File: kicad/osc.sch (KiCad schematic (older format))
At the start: 29 parts, among them J201 power, Q201 BC557, Q202 2N3819, U201 TL082, U202 TL082, U203 TL082

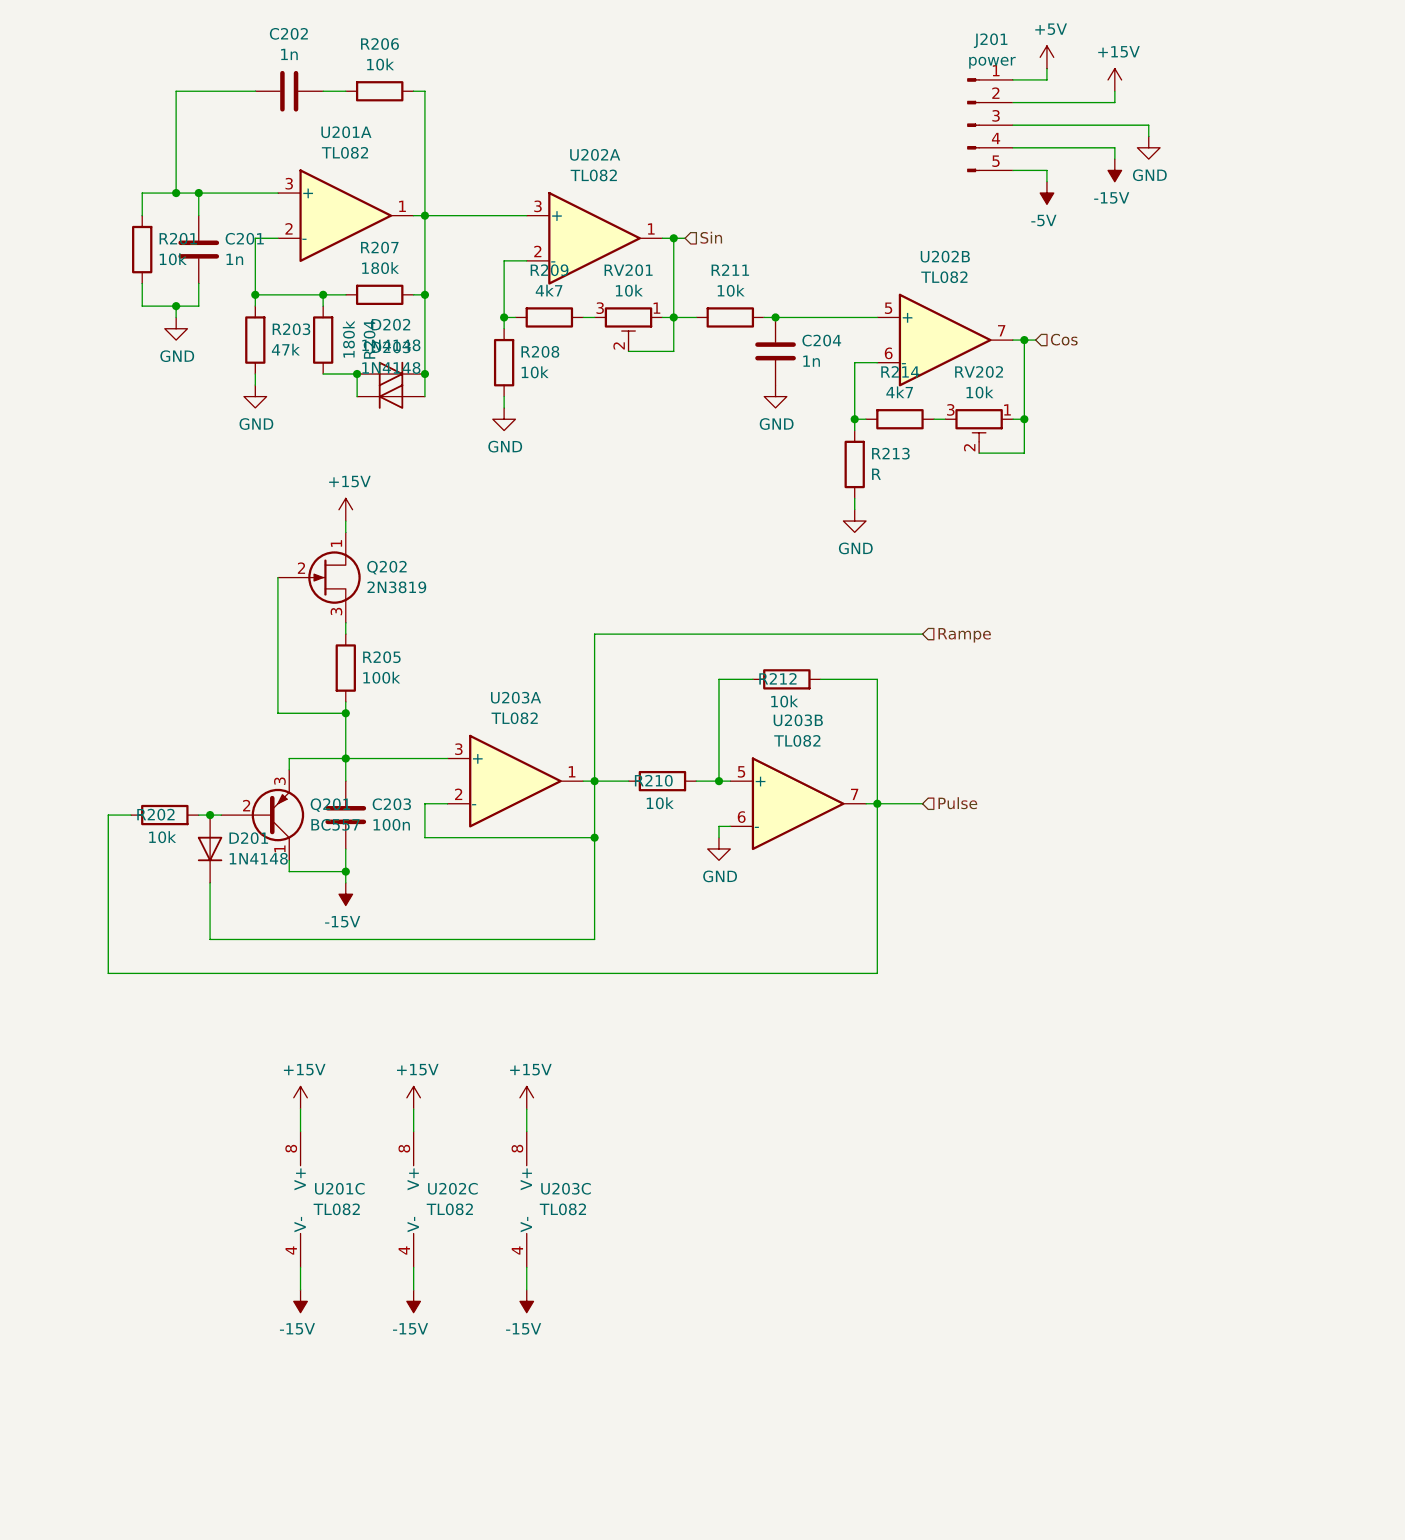
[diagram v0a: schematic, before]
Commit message: Tested oscillators
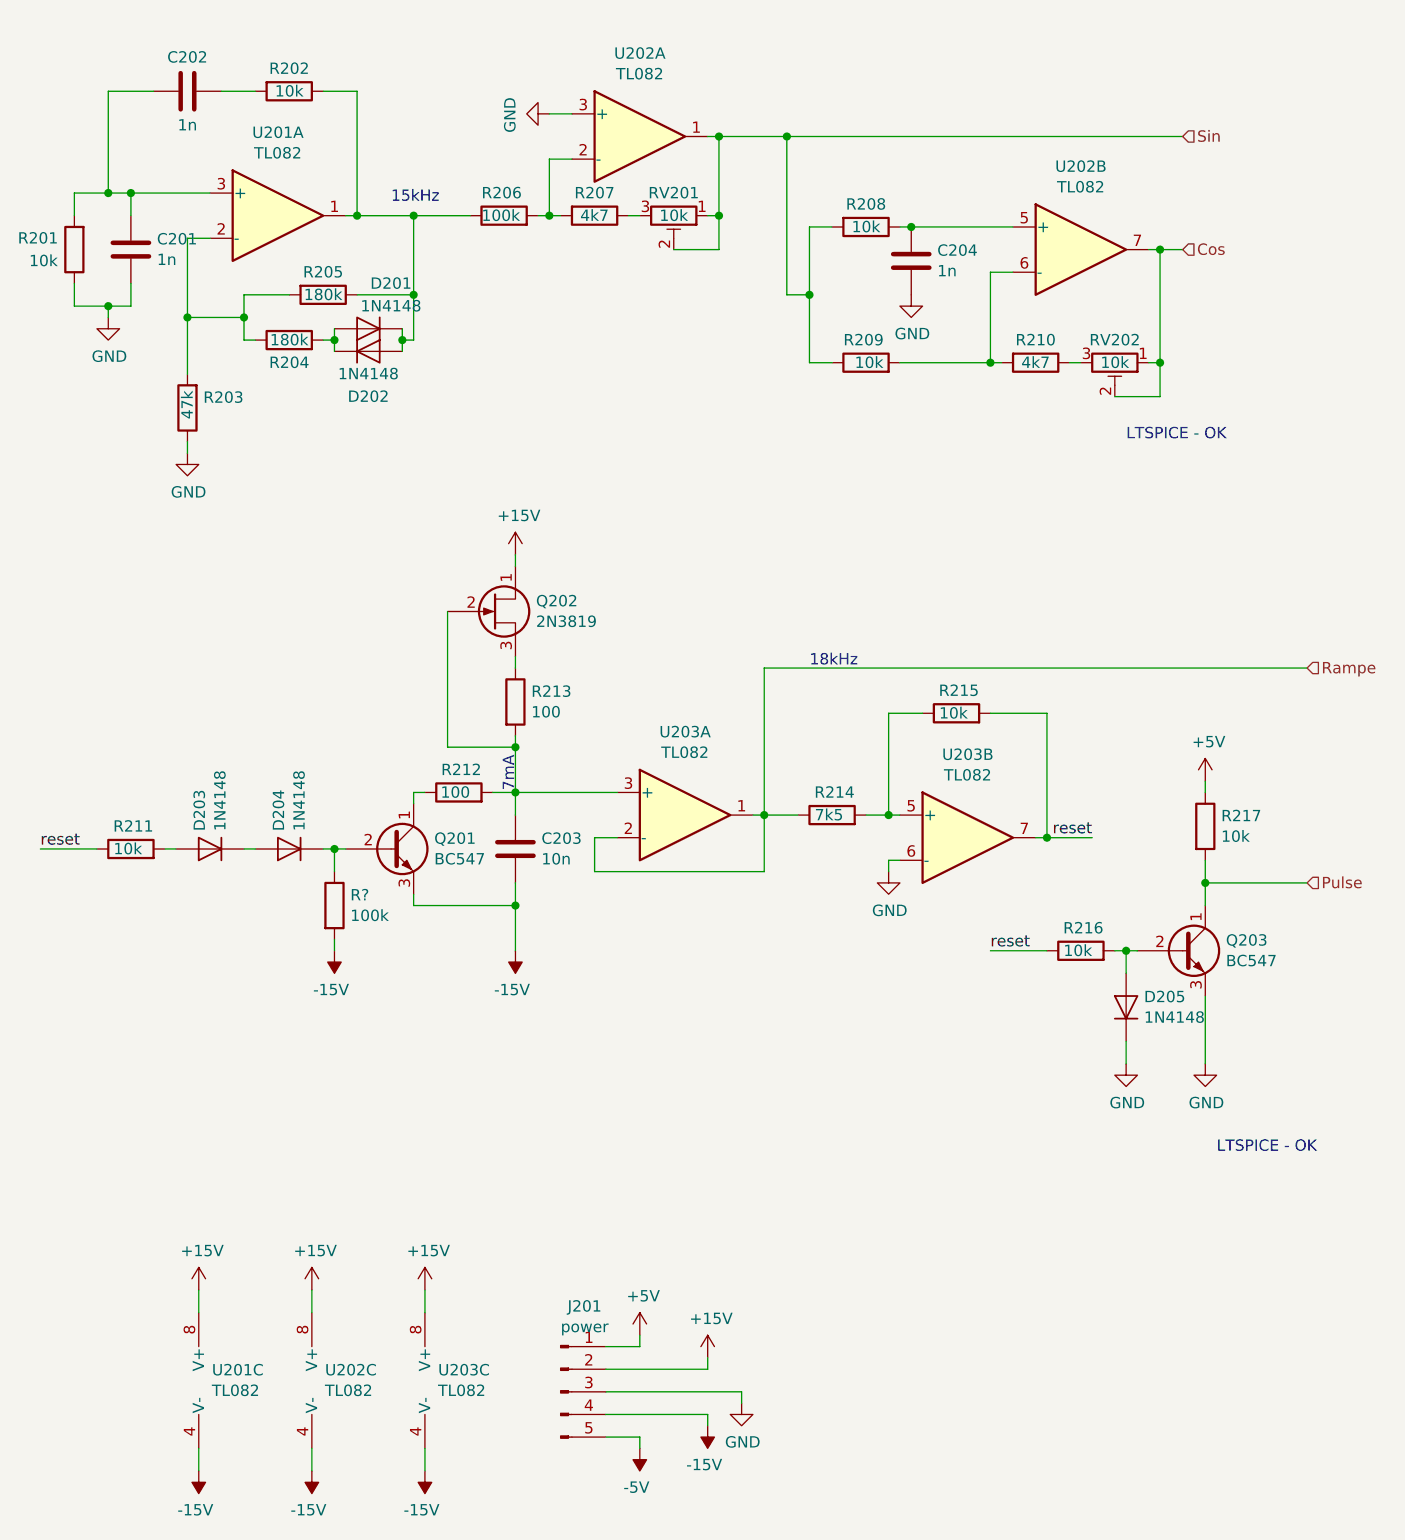
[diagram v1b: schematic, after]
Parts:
- removed Q201: BC557, Package_TO_SOT_THT:TO-92_Inline_Wide, symbol Transistor_BJT:BC557
- added D204, D205: 1N4148, Diode_THT:D_DO-35_SOD27_P7.62mm_Horizontal, symbol Diode:1N4148
- added Q201, Q203: BC547, Package_TO_SOT_THT:TO-92_Inline_Wide, symbol Transistor_BJT:BC547
- added R212: 100, Resistor_THT:R_Axial_DIN0204_L3.6mm_D1.6mm_P7.62mm_Horizontal, symbol Device:R
- added R216, R217: 10k, Resistor_THT:R_Axial_DIN0204_L3.6mm_D1.6mm_P7.62mm_Horizontal, symbol Device:R
- added R?: 100k, Resistor_THT:R_Axial_DIN0204_L3.6mm_D1.6mm_P7.62mm_Horizontal, symbol Device:R
- C203: value 100n -> 10n
- R206: renamed from R208; value 10k -> 100k
- R209: renamed from R213; value R -> 10k
- R213: renamed from R205; value 100k -> 100
- R214: renamed from R210; value 10k -> 7k5
- renumbered D202 to D201, D203 to D202, D201 to D203, R206 to R202, R207 to R205, R209 to R207, R211 to R208, R214 to R210, R202 to R211, R212 to R215
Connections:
- net +5V: now also R217.1
- net -15V: now also Q201.3 (E), R?.2
- net GND: now also U202.3 (+), D205.1 (K), Q203.3 (E); no longer R206.1, R209.1
- net Pulse: now also Q203.1 (C), R217.2; no longer R211.1, R215.2, U203.7
- net Rampe: no longer D203.1 (K)
- net Sin: now also R209.1
- net at D201.1 (K), D202.2 (A), R202.1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: now also R206.1; no longer U202.3 (+)
- net at R203.2, R205.2, U201.2 (-): now also R204.1; no longer R204.2
- net at D201.2 (A), D202.1 (K): now also R204.2; no longer R204.1
- net at C203.2, Q202.2 (G), R213.2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: now also R212.2
- new net: D203.1 (K), D204.2 (A)
- new net: Q201.1 (C), R212.1
- new net: D204.1 (K), Q201.2 (B), R?.1
- new net: D205.2 (A), Q203.2 (B), R216.2
- new net reset: R211.1, R215.2, R216.1, U203.7
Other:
- note added: "15kHz"
- note added: "18kHz"
- note added: "7mA"
- note added: "LTSPICE - OK"
- moved on the sheet: C201, C202, C203, C204, D201, D202, J201, Q202, R201, R202, R203, R204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

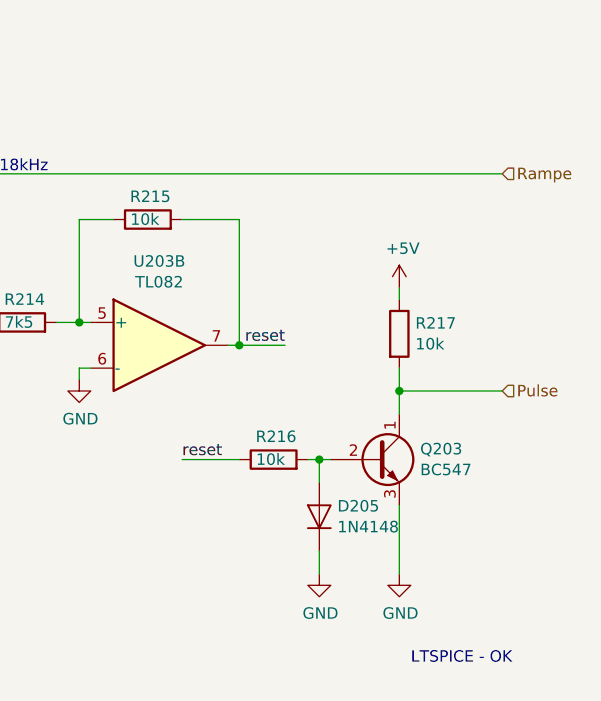
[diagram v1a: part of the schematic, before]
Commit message: Quick fix and documentation
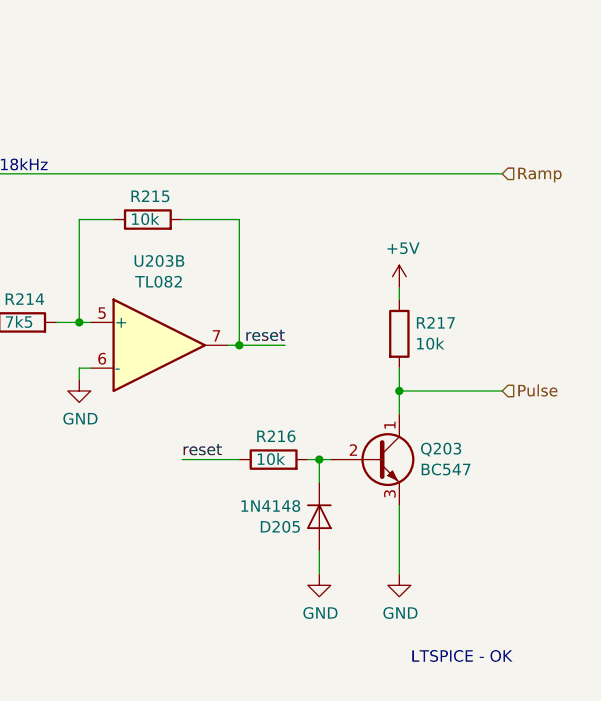
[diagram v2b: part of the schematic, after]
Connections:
- net GND: now also D205.2 (A); no longer D205.1 (K)
- net at Q203.2 (B), R216.2: now also D205.1 (K); no longer D205.2 (A)
- net Rampe renamed Ramp
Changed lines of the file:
@@
 Cos
 Text HLabel 6150 3500 2    50   Input ~ 0
-Rampe
+Ramp
 Text HLabel 6150 4450 2    50   Input ~ 0
 Pulse
@@
 F 3 "http://www.nxp.com/documents/data_sheet/1N4148_1N4448.pdf" H 5350 5000 50  0001 C CNN
 	1    5350 5000
-	0    -1   -1   0
-$EndComp
-$Comp
+	0    1    1    0
+$EndComp
+$Comp
